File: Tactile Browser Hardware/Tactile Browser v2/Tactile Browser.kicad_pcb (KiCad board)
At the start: 4 copper layers, 82.5 x 114 mm, 130 parts, among them SW1 SW_Push, SW10 SW_Push, SW11 SW_Push, SW12 SW_Push, SW13 SW_Push, SW14 SW_Push, SW15 SW_Push, SW16 SW_Push, SW17 SW_Push, SW18 SW_Push, SW2 SW_Push, SW3 SW_Push, SW4 SW_Push, SW5 SW_Push, SW6 SW_Push, SW7 SW_Push, SW8 SW_Push, SW9 SW_Push

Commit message: solenoid wiring!!
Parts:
- removed 5V_logic_rail1: Conn_01x01_Pin, TerminalBlock:TerminalBlock_Xinya_XY308-2.54-2P_1x02_P2.54mm_Horizontal
- removed I2C_bus1: Conn_01x02_Pin, TerminalBlock:TerminalBlock_Xinya_XY308-2.54-2P_1x02_P2.54mm_Horizontal
- removed Solenoid1, Solenoid10, Solenoid11, Solenoid12, Solenoid13, Solenoid14, Solenoid15, Solenoid16, Solenoid17, Solenoid18, Solenoid2, Solenoid3, Solenoid4, Solenoid5, Solenoid6, Solenoid7, Solenoid8, Solenoid9: Conn_01x02_Pin, TerminalBlock_Phoenix:ScrewTerminal_Vertical_1935310
- added 5V: Conn_01x01_Pin, Connector_JST:JST_PH_B2B-PH-SM4-TB_1x02-1MP_P2.00mm_Vertical, F.Cu at (88.9, 134.8)
- added I2C: Conn_01x02_Pin, Connector_JST:JST_PH_B2B-PH-SM4-TB_1x02-1MP_P2.00mm_Vertical, F.Cu at (89.1, 142.8)
- added Sol1: Conn_01x02_Pin, TerminalBlock_Phoenix:ScrewTerminal_Vertical_1935310, F.Cu at (43.5, 37.0)
- added Sol10: Conn_01x02_Pin, TerminalBlock_Phoenix:ScrewTerminal_Vertical_1935310, F.Cu at (113.3, 53.0)
- added Sol11: Conn_01x02_Pin, TerminalBlock_Phoenix:ScrewTerminal_Vertical_1935310, F.Cu at (113.3, 64.1)
- added Sol12: Conn_01x02_Pin, TerminalBlock_Phoenix:ScrewTerminal_Vertical_1935310, F.Cu at (113.3, 75.1)
- added Sol13: Conn_01x02_Pin, TerminalBlock_Phoenix:ScrewTerminal_Vertical_1935310, F.Cu at (113.5, 86.1)
- added Sol14: Conn_01x02_Pin, TerminalBlock_Phoenix:ScrewTerminal_Vertical_1935310, F.Cu at (113.3, 97.1)
- added Sol15: Conn_01x02_Pin, TerminalBlock_Phoenix:ScrewTerminal_Vertical_1935310, F.Cu at (113.0, 108.0)
- added Sol16: Conn_01x02_Pin, TerminalBlock_Phoenix:ScrewTerminal_Vertical_1935310, F.Cu at (113.0, 119.1)
- added Sol17: Conn_01x02_Pin, TerminalBlock_Phoenix:ScrewTerminal_Vertical_1935310, F.Cu at (113.0, 130.1)
- added Sol18: Conn_01x02_Pin, TerminalBlock_Phoenix:ScrewTerminal_Vertical_1935310, F.Cu at (113.0, 141.1)
- added Sol2: Conn_01x02_Pin, TerminalBlock_Phoenix:ScrewTerminal_Vertical_1935310, F.Cu at (43.5, 47.5)
- added Sol3: Conn_01x02_Pin, TerminalBlock_Phoenix:ScrewTerminal_Vertical_1935310, F.Cu at (43.5, 58.5)
- added Sol4: Conn_01x02_Pin, TerminalBlock_Phoenix:ScrewTerminal_Vertical_1935310, F.Cu at (43.5, 69.5)
- added Sol5: Conn_01x02_Pin, TerminalBlock_Phoenix:ScrewTerminal_Vertical_1935310, F.Cu at (43.5, 80.5)
- added Sol6: Conn_01x02_Pin, TerminalBlock_Phoenix:ScrewTerminal_Vertical_1935310, F.Cu at (43.5, 91.5)
- added Sol7: Conn_01x02_Pin, TerminalBlock_Phoenix:ScrewTerminal_Vertical_1935310, F.Cu at (43.5, 102.5)
- added Sol8: Conn_01x02_Pin, TerminalBlock_Phoenix:ScrewTerminal_Vertical_1935310, F.Cu at (43.5, 113.5)
- added Sol9: Conn_01x02_Pin, TerminalBlock_Phoenix:ScrewTerminal_Vertical_1935310, F.Cu at (113.3, 42.0)
- 100nF1, 100nF10, 100nF11, 100nF12, 100nF13, 100nF14, 100nF15, 100nF2, 100nF3, 100nF4, 100nF5, 100nF6, 100nF7, 100nF8, 100nF9, C2_100nF1, C2_100nF2, C2_100nF3, DS10, DS11, DS12, DS13, DS14, DS15, DS16, DS17, DS18, DS19, DS20, DS21, DS22, DS23, DS24, DS25, DS26, DS27, DS28, DS29, DS30, DS31, DS32, DS33, DS34, DS35, DS36, DS7, DS8, DS9: moved to F.Cu
- 12V_supply1: footprint TerminalBlock_Altech:Altech_AK100_1x02_P5.00mm -> TerminalBlock_Phoenix:ScrewTerminal_Vertical_1935310
- moved DS2 138.2 mm to (39.5, 38.0), turned to -90 degrees
- moved DS4 136.7 mm to (40.0, 50.0), turned to 90 degrees
- moved DS6 136.2 mm to (40.0, 60.5), turned to -90 degrees
- moved DS1 129.4 mm to (47.0, 38.5), turned to -90 degrees
- moved DS3 129.0 mm to (46.5, 50.0), turned to -90 degrees
- moved DS5 128.1 mm to (47.0, 60.5), turned to -90 degrees
- moved 100nF1 83.7 mm to (63.0, 45.0), turned to -90 degrees
- moved D5 77.3 mm to (69.5, 115.5), turned to 90 degrees
- moved 100uf25V1 73.2 mm to (73.5, 40.5), turned to -90 degrees
- moved SW5 72.9 mm to (66.0, 111.5), turned to 0 degrees
- moved SW6 71.4 mm to (66.0, 119.5), turned to 180 degrees
- moved 1000uf25V4 70.5 mm to (73.5, 54.5), turned to -90 degrees
- moved D6 68.8 mm to (62.5, 115.5), turned to -90 degrees
- moved SW3 65.3 mm to (66.0, 94.0)
- moved D3 65.0 mm to (69.5, 98.0), turned to 90 degrees
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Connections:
- net Enable renamed STBY
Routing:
- net Row1: track 112.7 -> 1.00 mm
- net Row4: track 91.0 -> 0.00 mm
- net Col1: track 84.1 -> 0.30 mm
- net Col2: track 66.8 -> 0.00 mm
- net Row2: track 62.0 -> 1.54 mm
- net Row3: track 42.2 -> 0.00 mm
- net Col3: track 42.0 -> 0.00 mm
- net S1_out2: track 0.19 -> 25.8 mm, vias 0 -> 1
- net Row6: track 25.1 -> 0.00 mm
- net 12V: track 0.00 -> 18.8 mm
- net S2_out1: track 0.29 -> 19.0 mm
- net S2_out2: track 0.00 -> 18.4 mm, vias 0 -> 1
- net Net-(D11-A): track 16.3 -> 0.00 mm
- net S1_out1: track 0.00 -> 15.5 mm, vias 0 -> 1
- net Net-(D1-A): track 14.6 -> 0.00 mm
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
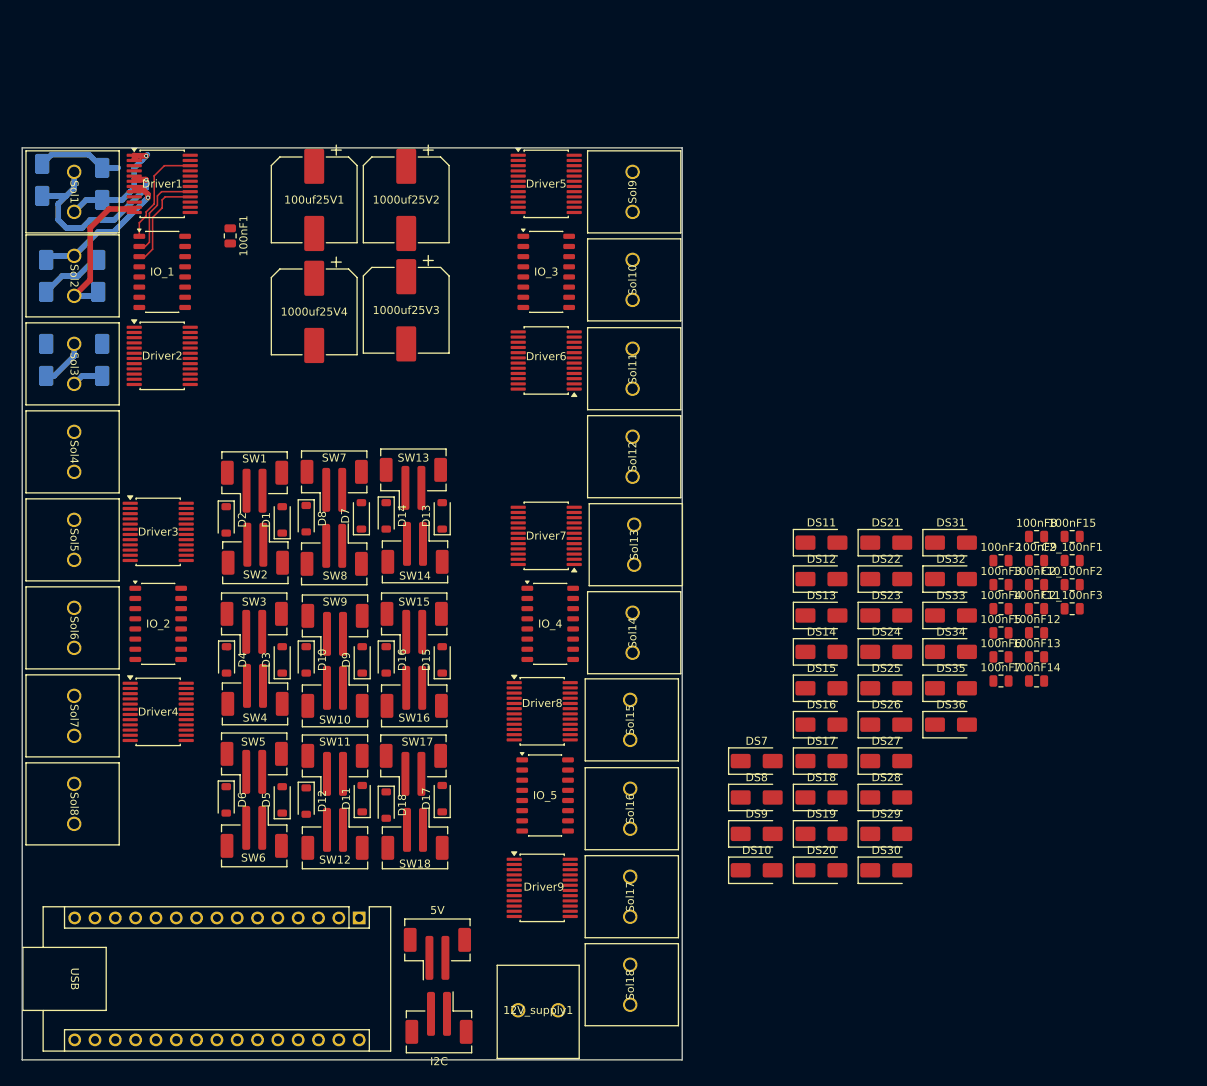
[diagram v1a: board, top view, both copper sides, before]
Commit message: made the board even smaller!
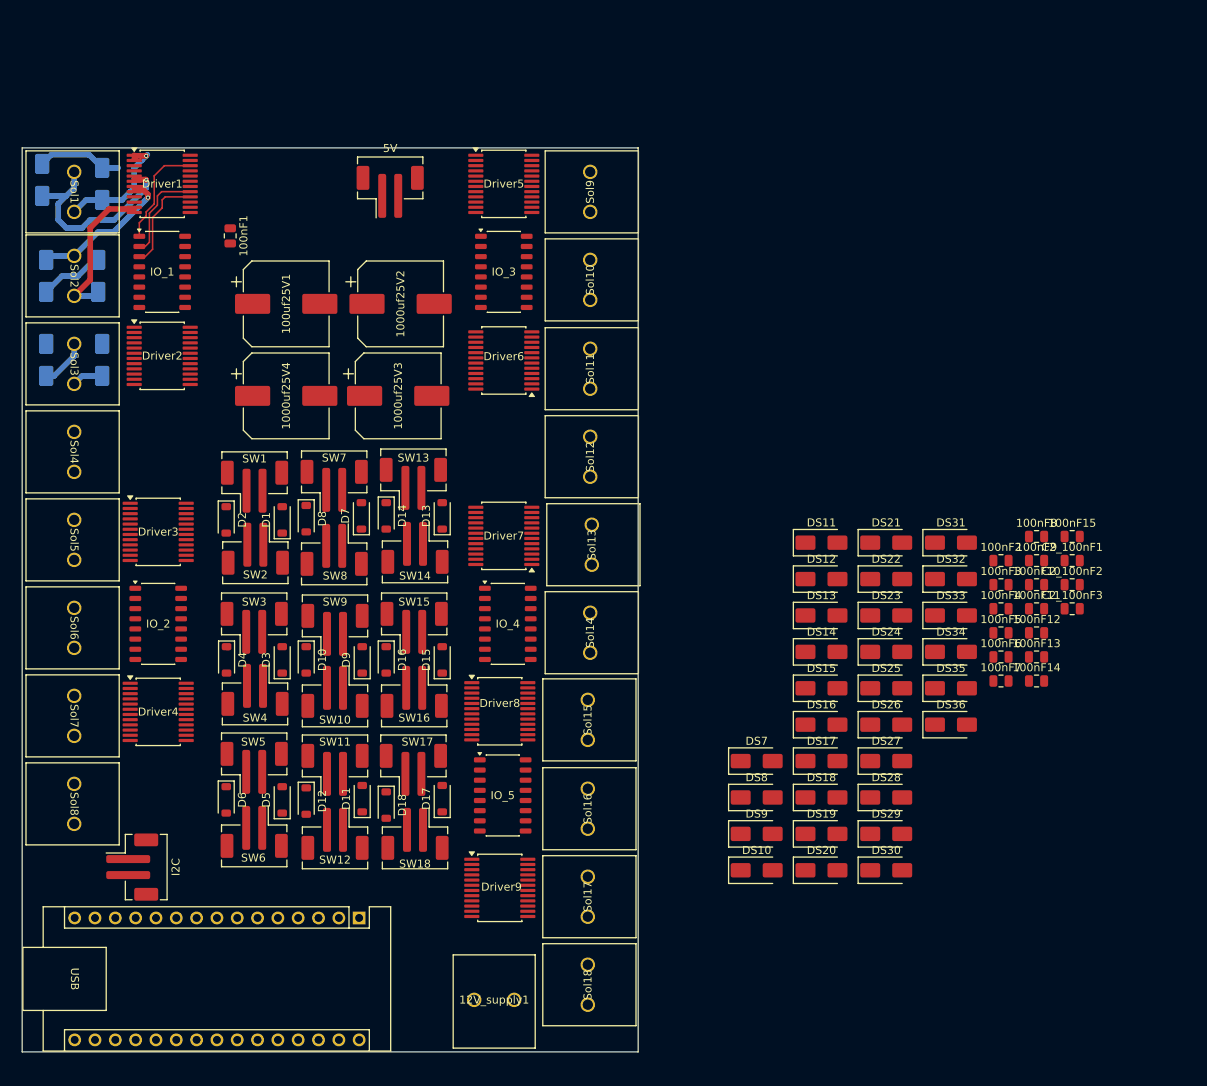
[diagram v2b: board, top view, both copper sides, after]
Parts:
- moved 5V 95.4 mm to (83.0, 39.5)
- moved I2C 42.7 mm to (50.8, 123.9), turned to -90 degrees
- moved 100uf25V1 13.5 mm to (70.0, 53.5), turned to 0 degrees
- moved 1000uf25V2 13.0 mm to (84.3, 53.5), turned to 0 degrees
- moved 1000uf25V4 11.1 mm to (70.0, 65.0), turned to 0 degrees
- moved 1000uf25V3 10.7 mm to (84.0, 65.0), turned to 0 degrees
- moved 12V_supply1 5.65 mm to (93.5, 140.5)
- moved Driver5 5.30 mm to (97.2, 38.5)
- moved Driver6 5.30 mm to (97.2, 60.6)
- moved Driver7 5.30 mm to (97.2, 82.5)
- moved Driver8 5.30 mm to (96.7, 104.4)
- moved Driver9 5.30 mm to (96.7, 126.5)
- moved IO_3 5.30 mm to (97.2, 49.5)
- moved IO_4 5.30 mm to (97.7, 93.5)
- moved IO_5 5.30 mm to (97.1, 114.9)
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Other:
- board size 82.5 x 114 mm -> 77 x 113 mm

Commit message: capacitor naming scheme
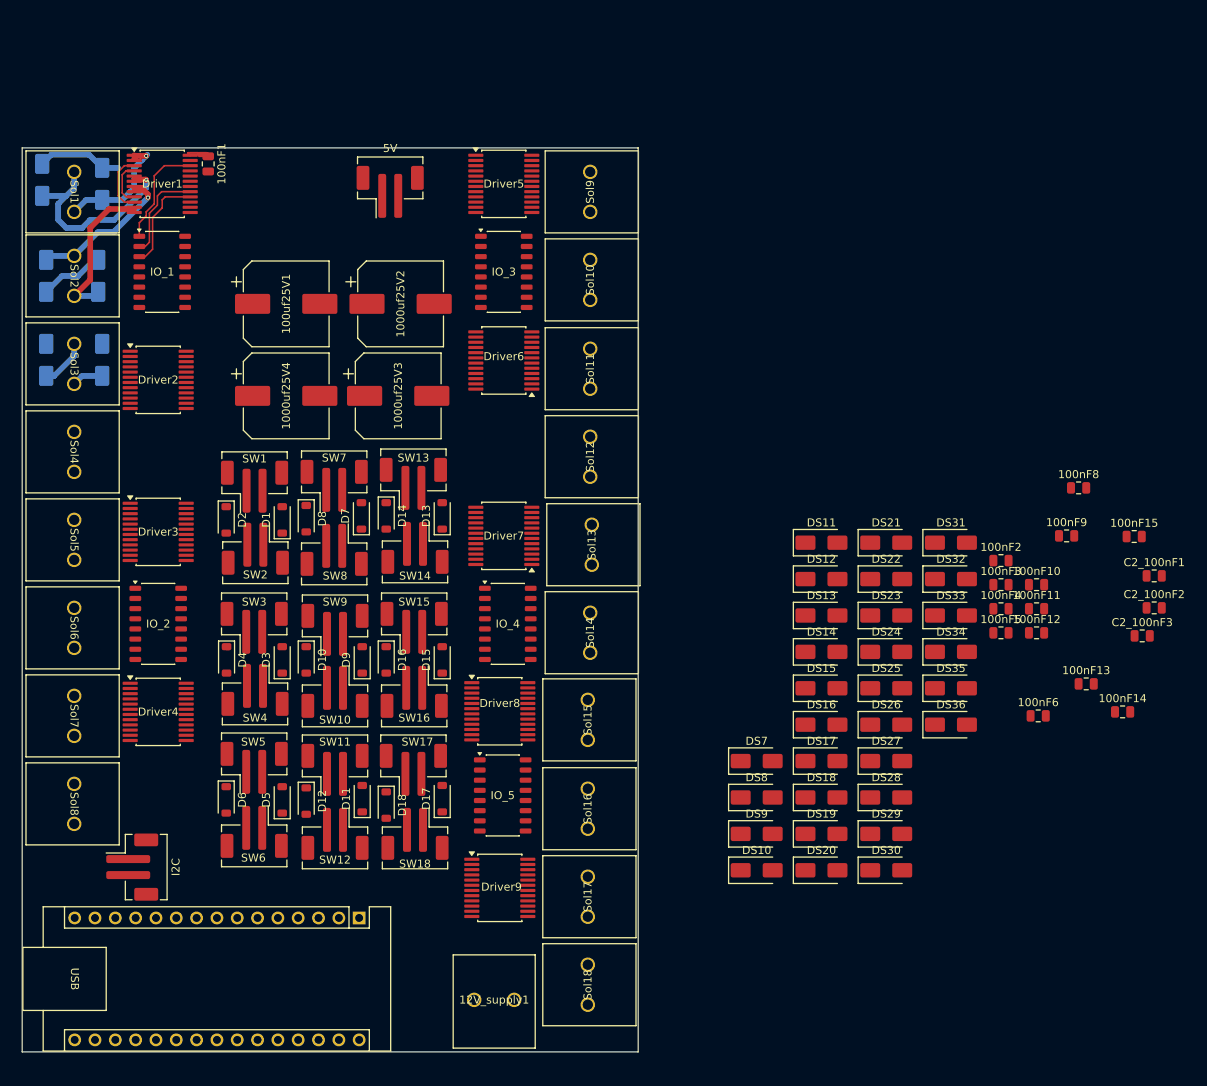
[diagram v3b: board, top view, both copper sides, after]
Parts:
- removed 100nF7: C, Capacitor_SMD:C_0805_2012Metric
- moved 100nF14 11.4 mm to (174.6, 104.5)
- moved C2_100nF2 10.7 mm to (178.5, 91.5)
- moved C2_100nF1 10.4 mm to (178.5, 87.5)
- moved 100nF1 9.41 mm to (60.2, 36.0)
- moved C2_100nF3 9.39 mm to (177.0, 95.0)
- moved 100nF6 8.72 mm to (164.0, 105.0)
- moved 100nF8 8.04 mm to (169.1, 76.5)
- moved 100nF15 7.75 mm to (176.0, 82.6)
- moved 100nF13 7.06 mm to (170.0, 101.0)
- moved 100nF9 4.86 mm to (167.6, 82.5)
- moved Driver2 3.04 mm to (54.0, 63.0)
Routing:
- net GND: track 0.00 -> 13.3 mm
- net 12V: track 18.8 -> 21.9 mm

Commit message: schottky diode placement
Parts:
- removed 100nF10, 100nF11, 100nF12, 100nF13, 100nF14, 100nF15, 100nF3, 100nF4, 100nF5, 100nF6, 100nF8, 100nF9, C2_100nF1, C2_100nF2, C2_100nF3: C, Capacitor_SMD:C_0805_2012Metric
- added 100uF1: C, Capacitor_SMD:C_0805_2012Metric, F.Cu at (139.9, 27.4)
- added 100uF10: C, Capacitor_SMD:C_0805_2012Metric, F.Cu at (144.3, 30.4)
- added 100uF11: C, Capacitor_SMD:C_0805_2012Metric, F.Cu at (144.3, 33.5)
- added 100uF12: C, Capacitor_SMD:C_0805_2012Metric, F.Cu at (144.3, 36.5)
- added 100uF13: C, Capacitor_SMD:C_0805_2012Metric, F.Cu at (144.3, 39.5)
- added 100uF14: C, Capacitor_SMD:C_0805_2012Metric, F.Cu at (144.3, 42.5)
- added 100uF15: C, Capacitor_SMD:C_0805_2012Metric, F.Cu at (148.8, 24.4)
- added 100uF16: C, Capacitor_SMD:C_0805_2012Metric, F.Cu at (148.8, 27.4)
- added 100uF17: C, Capacitor_SMD:C_0805_2012Metric, F.Cu at (148.8, 30.4)
- added 100uF18: C, Capacitor_SMD:C_0805_2012Metric, F.Cu at (148.8, 33.5)
- added 100uF2: C, Capacitor_SMD:C_0805_2012Metric, F.Cu at (139.9, 30.4)
- added 100uF3: C, Capacitor_SMD:C_0805_2012Metric, F.Cu at (123.0, 26.8)
- added 100uF4: C, Capacitor_SMD:C_0805_2012Metric, F.Cu at (139.9, 33.5)
- added 100uF5: C, Capacitor_SMD:C_0805_2012Metric, F.Cu at (139.9, 36.5)
- added 100uF6: C, Capacitor_SMD:C_0805_2012Metric, F.Cu at (139.9, 39.5)
- added 100uF7: C, Capacitor_SMD:C_0805_2012Metric, F.Cu at (139.9, 42.5)
- added 100uF8: C, Capacitor_SMD:C_0805_2012Metric, F.Cu at (141.2, 20.5)
- added 100uF9: C, Capacitor_SMD:C_0805_2012Metric, F.Cu at (144.3, 27.4)
- 100nF1, 100nF2, DS10, DS11, DS12, DS13, DS14, DS15, DS16, DS17, DS18, DS19, DS20, DS21, DS22, DS23, DS24, DS25, DS26, DS27, DS28, DS29, DS30, DS31, DS32, DS33, DS34, DS35, DS36, DS7, DS8, DS9: moved to B.Cu
- moved 100nF2 110.8 mm to (60.2, 36.0), turned to -90 degrees
- moved DS8 98.8 mm to (40.0, 72.0), turned to -90 degrees
- moved DS10 98.0 mm to (40.0, 82.8), turned to -90 degrees
- moved DS16 97.4 mm to (40.0, 115.8), turned to -90 degrees
- moved DS14 97.2 mm to (40.0, 105.0), turned to -90 degrees
- moved DS12 97.1 mm to (40.0, 94.0), turned to -90 degrees
- moved DS15 91.3 mm to (46.8, 115.8), turned to -90 degrees
- moved DS13 91.0 mm to (46.8, 105.0), turned to -90 degrees
- moved DS11 90.8 mm to (46.8, 93.8), turned to -90 degrees
- moved DS7 90.7 mm to (46.8, 72.0), turned to -90 degrees
- moved DS9 90.0 mm to (46.8, 82.8), turned to -90 degrees
- moved DS18 79.8 mm to (111.5, 39.5), turned to -90 degrees
- moved DS20 78.1 mm to (111.2, 50.5), turned to -90 degrees
- moved DS17 78.1 mm to (104.8, 39.5), turned to -90 degrees
- moved DS19 76.2 mm to (105.0, 50.5), turned to -90 degrees
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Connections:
- 100nF1 pad 1: 12V -> GND
- 100nF1 pad 2: GND -> 5V
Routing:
- net 5V: track 0.00 -> 13.5 mm, vias 0 -> 2
- net S1_in1: track 0.00 -> 12.4 mm, vias 0 -> 2
- net GND: track 13.3 -> 22.1 mm, vias 0 -> 2
- net PWM: track 0.00 -> 7.56 mm
- net 12V: track 21.9 -> 25.7 mm, vias 0 -> 2
- net STBY: track 0.00 -> 1.28 mm, vias 0 -> 1
